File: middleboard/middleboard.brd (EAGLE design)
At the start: 8 x 76.2 mm, 11 parts, among them P1 PAD, P2 PAD, P3 PAD, P4 PAD, Q1 SIA436DJ

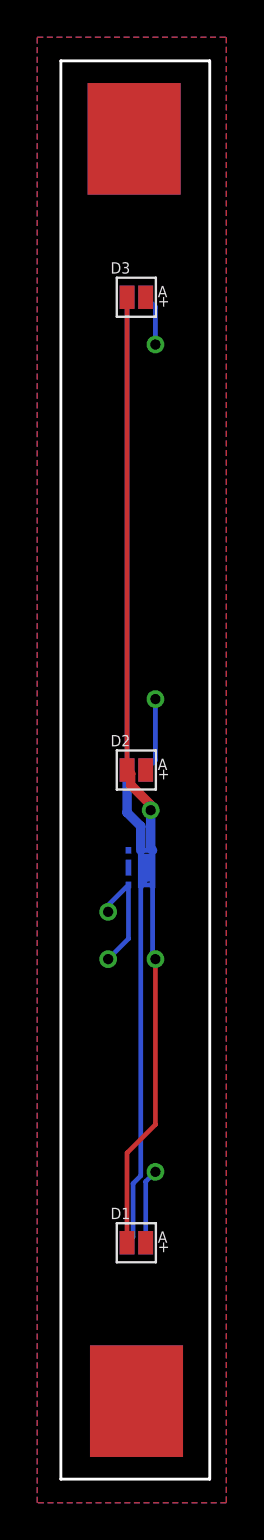
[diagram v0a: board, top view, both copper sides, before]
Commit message: Increased via sizes
Increased via sizes in bottom and
middle boards so we can solder wires in them.
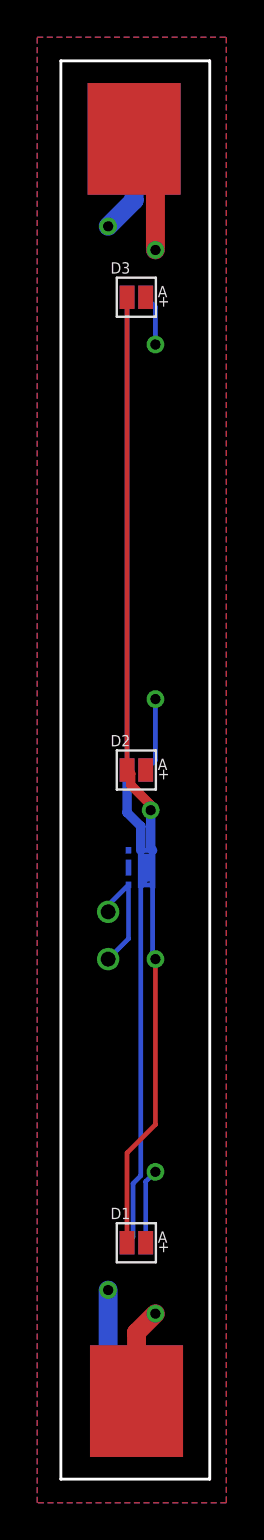
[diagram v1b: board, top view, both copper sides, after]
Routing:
- net GND: track 0.00 -> 11.9 mm, vias 0 -> 2
- net VCC: track 10.8 -> 22.4 mm, vias 3 -> 5
- added copper zone on layer 15, net GND
- added copper zone on layer 2, net VCC
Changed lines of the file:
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@@
 <layers>
 <layer number="1" name="Top" color="4" fill="1" visible="yes" active="yes"/>
-<layer number="2" name="Route2" color="16" fill="1" visible="no" active="yes"/>
+<layer number="2" name="Route2" color="16" fill="1" visible="yes" active="yes"/>
 <layer number="3" name="Route3" color="17" fill="1" visible="no" active="no"/>
 <layer number="4" name="Route4" color="18" fill="1" visible="no" active="no"/>
@@
 <layer number="13" name="Route13" color="21" fill="1" visible="no" active="no"/>
 <layer number="14" name="Route14" color="22" fill="1" visible="no" active="no"/>
-<layer number="15" name="Route15" color="23" fill="1" visible="no" active="yes"/>
+<layer number="15" name="Route15" color="23" fill="1" visible="yes" active="yes"/>
 <layer number="16" name="Bottom" color="1" fill="1" visible="yes" active="yes"/>
 <layer number="17" name="Pads" color="2" fill="1" visible="yes" active="yes"/>
@@
 <wire x1="4.556759375" y1="12.7" x2="4.556759375" y2="15.986759375" width="0.254" layer="16"/>
 <wire x1="4.556759375" y1="15.986759375" x2="5.08" y2="16.51" width="0.254" layer="16"/>
+<polygon width="0.1524" layer="2">
+<vertex x="-1.27" y="-1.27"/>
+<vertex x="-1.27" y="77.47"/>
+<vertex x="8.89" y="77.47"/>
+<vertex x="8.89" y="-1.27"/>
+</polygon>
+<via x="5.08" y="66.04" extent="1-16" drill="0.55"/>
+<via x="5.08" y="8.89" extent="1-16" drill="0.55"/>
+<wire x1="4.064" y1="4.191" x2="4.064" y2="7.874" width="1.016" layer="1"/>
+<wire x1="4.064" y1="7.874" x2="5.08" y2="8.89" width="1.016" layer="1"/>
+<wire x1="5.08" y1="66.04" x2="5.08" y2="70.866" width="1.016" layer="1"/>
+<wire x1="5.08" y1="70.866" x2="3.937" y2="72.009" width="1.016" layer="1"/>
 </signal>
 <signal name="GND">
@@
 <vertex x="8.89" y="-1.27"/>
 </polygon>
+<polygon width="0.1524" layer="15">
+<vertex x="-1.27" y="-1.27"/>
+<vertex x="-1.27" y="77.47"/>
+<vertex x="8.89" y="77.47"/>
+<vertex x="8.89" y="-1.27"/>
+</polygon>
+<via x="2.54" y="67.31" extent="1-16" drill="0.55"/>
+<via x="2.54" y="10.16" extent="1-16" drill="0.55"/>
+<wire x1="2.54" y1="10.16" x2="2.54" y2="5.715" width="1.016" layer="16"/>
+<wire x1="2.54" y1="5.715" x2="4.064" y2="4.191" width="1.016" layer="16"/>
+<wire x1="3.937" y1="72.009" x2="3.937" y2="68.707" width="1.016" layer="16"/>
+<wire x1="3.937" y1="68.707" x2="2.54" y2="67.31" width="1.016" layer="16"/>
 </signal>
 <signal name="N$3">
@@
 <signal name="P">
 <contactref element="Q1" pad="P$4"/>
-<via x="2.54" y="30.48" extent="1-16" drill="0.55"/>
-<via x="2.54" y="27.94" extent="1-16" drill="0.55"/>
+<via x="2.54" y="30.48" extent="1-16" drill="0.8"/>
+<via x="2.54" y="27.94" extent="1-16" drill="0.8"/>
 <wire x1="3.6322" y1="31.9278" x2="2.54" y2="30.8356" width="0.254" layer="16"/>
 <wire x1="2.54" y1="30.8356" x2="2.54" y2="30.48" width="0.254" layer="16"/>
